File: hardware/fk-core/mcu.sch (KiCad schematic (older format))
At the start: 10 parts, among them P2 CONN_01X02, SW1 SPST-RESCUE-mcu, U1 ATSAMD21G-M, X1 XTAL-3.2X1.5

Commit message: Adding GPS connector and BOM placeholder.
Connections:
- net GPS_RX: now reaches U1.37 (PB22(SER5:2+))
- net GPX_TS: now reaches U1.38 (PB23(SER5:3+))
- no-connect marks 26 -> 24
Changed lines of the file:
@@
 LIBS:tps63060
 LIBS:max1704xx
+LIBS:gp-635tsmd
 LIBS:fk-core-cache
 EELAYER 25 0
@@
 	2350 2700 2400 2700
 $Comp
-L GND #PWR4
+L GND #PWR01
 U 1 1 587F9BAD
 P 2850 1900
-F 0 "#PWR4" H 2850 1650 50  0001 C CNN
+F 0 "#PWR01" H 2850 1650 50  0001 C CNN
 F 1 "GND" H 2850 1750 50  0000 C CNN
 F 2 "" H 2850 1900 50  0000 C CNN
@@
 $EndComp
 $Comp
-L GND #PWR3
+L GND #PWR02
 U 1 1 587F9BCB
 P 2350 1900
-F 0 "#PWR3" H 2350 1650 50  0001 C CNN
+F 0 "#PWR02" H 2350 1650 50  0001 C CNN
 F 1 "GND" H 2350 1750 50  0000 C CNN
 F 2 "" H 2350 1900 50  0000 C CNN
@@
 Connection ~ 2350 2700
 $Comp
-L +3V3 #PWR5
+L +3V3 #PWR03
 U 1 1 587F9D09
 P 3350 1900
-F 0 "#PWR5" H 3350 1750 50  0001 C CNN
+F 0 "#PWR03" H 3350 1750 50  0001 C CNN
 F 1 "+3V3" H 3350 2040 50  0000 C CNN
 F 2 "" H 3350 1900 50  0000 C CNN
@@
 	3700 2550 3700 2650
 $Comp
-L GND #PWR6
+L GND #PWR04
 U 1 1 587F9D9D
 P 3700 3000
-F 0 "#PWR6" H 3700 2750 50  0001 C CNN
+F 0 "#PWR04" H 3700 2750 50  0001 C CNN
 F 1 "GND" H 3700 2850 50  0000 C CNN
 F 2 "" H 3700 3000 50  0000 C CNN
@@
 	3300 1450 3800 1450
 $Comp
-L GND #PWR8
+L GND #PWR05
 U 1 1 587F9FB0
 P 5150 1450
-F 0 "#PWR8" H 5150 1200 50  0001 C CNN
+F 0 "#PWR05" H 5150 1200 50  0001 C CNN
 F 1 "GND" H 5150 1300 50  0000 C CNN
 F 2 "" H 5150 1450 50  0000 C CNN
@@
 	5150 1450 4800 1450
 $Comp
-L +3V3 #PWR9
+L +3V3 #PWR06
 U 1 1 587FA095
 P 7250 1900
-F 0 "#PWR9" H 7250 1750 50  0001 C CNN
+F 0 "#PWR06" H 7250 1750 50  0001 C CNN
 F 1 "+3V3" H 7250 2040 50  0000 C CNN
 F 2 "" H 7250 1900 50  0000 C CNN
@@
 	6900 2650 7750 2650
 $Comp
-L GND #PWR7
+L GND #PWR07
 U 1 1 587FABBF
 P 3750 5650
-F 0 "#PWR7" H 3750 5400 50  0001 C CNN
+F 0 "#PWR07" H 3750 5400 50  0001 C CNN
 F 1 "GND" H 3750 5500 50  0000 C CNN
 F 2 "" H 3750 5650 50  0000 C CNN
@@
 SCL1
 $Comp
-L +3V3 #PWR10
+L +3V3 #PWR08
 U 1 1 587FE0E2
 P 9850 3800
-F 0 "#PWR10" H 9850 3650 50  0001 C CNN
+F 0 "#PWR08" H 9850 3650 50  0001 C CNN
 F 1 "+3V3" H 9850 3940 50  0000 C CNN
 F 2 "" H 9850 3800 50  0000 C CNN
@@
 $EndComp
 $Comp
-L +3V3 #PWR11
+L +3V3 #PWR09
 U 1 1 587FE165
 P 9850 4000
-F 0 "#PWR11" H 9850 3850 50  0001 C CNN
+F 0 "#PWR09" H 9850 3850 50  0001 C CNN
 F 1 "+3V3" H 9850 4140 50  0000 C CNN
 F 2 "" H 9850 4000 50  0000 C CNN
@@
 NoConn ~ 6900 4450
 NoConn ~ 6900 4550
-NoConn ~ 7700 5250
-NoConn ~ 7700 5150
 NoConn ~ 4200 4650
 NoConn ~ 4200 4550
@@
 NoConn ~ 4200 3750
 $Comp
-L PWR_FLAG #FLG1
+L PWR_FLAG #FLG010
 U 1 1 5880FC74
 P 3300 1300
-F 0 "#FLG1" H 3300 1395 50  0001 C CNN
+F 0 "#FLG010" H 3300 1395 50  0001 C CNN
 F 1 "PWR_FLAG" H 3300 1480 50  0000 C CNN
 F 2 "" H 3300 1300 50  0000 C CNN
@@
 $EndComp
 $Comp
-L +3V3 #PWR1
+L +3V3 #PWR011
 U 1 1 58811F88
 P 1800 1900
-F 0 "#PWR1" H 1800 1750 50  0001 C CNN
+F 0 "#PWR011" H 1800 1750 50  0001 C CNN
 F 1 "+3V3" H 1800 2040 50  0000 C CNN
 F 2 "" H 1800 1900 50  0000 C CNN
@@
 $EndComp
 $Comp
-L GND #PWR2
+L GND #PWR012
 U 1 1 58811FC0
 P 1800 2700
-F 0 "#PWR2" H 1800 2450 50  0001 C CNN
+F 0 "#PWR012" H 1800 2450 50  0001 C CNN
 F 1 "GND" H 1800 2550 50  0000 C CNN
 F 2 "" H 1800 2700 50  0000 C CNN
@@
 $EndComp
 NoConn ~ 6900 3350
+Text GLabel 7700 5150 2    60   Input ~ 0
+GPS_RX
+Text GLabel 7700 5250 2    60   Input ~ 0
+GPX_TS
 $EndSCHEMATC

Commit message: Assigning most of the footprints.
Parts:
- C1, C10, C2, C3: footprint (none) -> Capacitors_SMD:C_0805_HandSoldering
- P2: footprint (none) -> Socket_Strips:Socket_Strip_Straight_1x02
- R1, R2: footprint (none) -> Resistors_SMD:R_0805_HandSoldering
- SW1: footprint (none) -> Buttons_Switches_SMD:SW_SPST_KMR2
- U1: footprint SparkFun-DigitalIC_QFN-48 -> Housings_QFP:TQFP-48-1EP_7x7mm_Pitch0.5mm
- X1: footprint XTAL3215 -> Crystals:Crystal_SMD_G8-2pin_3.2x1.5mm_HandSoldering
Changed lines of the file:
@@
 F 0 "U1" H 4300 5860 45  0000 L BNN
 F 1 "ATSAMD21G-M" H 4300 2740 45  0000 L BNN
-F 2 "SparkFun-DigitalIC_QFN-48" H 5530 4200 20  0001 C CNN
+F 2 "Housings_QFP:TQFP-48-1EP_7x7mm_Pitch0.5mm" H 5530 4200 20  0001 C CNN
 F 3 "http://www.atmel.com/Images/Atmel-42181-SAM-D21_Datasheet.pdf" H 5500 4050 60  0001 C CNN
 F 4 "ATSAMD21G18A-AUTCT-ND" H 5500 4050 60  0001 C CNN "SPN"
@@
 F 0 "X1" H 2500 2850 45  0000 L BNN
 F 1 "XTAL-3.2X1.5" H 2450 2500 45  0000 L BNN
-F 2 "XTAL3215" H 2630 2850 20  0001 C CNN
+F 2 "Crystals:Crystal_SMD_G8-2pin_3.2x1.5mm_HandSoldering" H 2630 2850 20  0001 C CNN
 F 3 "" H 2600 2700 60  0001 C CNN
 F 4 "644-1156-1-ND" H 2600 2700 60  0001 C CNN "SPN"
@@
 F 0 "C1" H 2375 2350 50  0000 L CNN
 F 1 "22pF" H 2375 2150 50  0000 L CNN
-F 2 "" H 2388 2100 50  0000 C CNN
+F 2 "Capacitors_SMD:C_0805_HandSoldering" H 2388 2100 50  0001 C CNN
 F 3 "" H 2350 2250 50  0000 C CNN
 F 4 "399-1113-1-ND" H 2350 2250 60  0001 C CNN "SPN"
@@
 F 0 "C2" H 2875 2350 50  0000 L CNN
 F 1 "22pF" H 2875 2150 50  0000 L CNN
-F 2 "" H 2888 2100 50  0000 C CNN
+F 2 "Capacitors_SMD:C_0805_HandSoldering" H 2888 2100 50  0001 C CNN
 F 3 "" H 2850 2250 50  0000 C CNN
 F 4 "399-1113-1-ND" H 2850 2250 60  0001 C CNN "SPN"
@@
 F 0 "C3" H 3725 2900 50  0000 L CNN
 F 1 "1uF" H 3725 2700 50  0000 L CNN
-F 2 "" H 3738 2650 50  0000 C CNN
+F 2 "Capacitors_SMD:C_0805_HandSoldering" H 3738 2650 50  0001 C CNN
 F 3 "" H 3700 2800 50  0000 C CNN
 F 4 "490-1320-1-ND" H 3700 2800 60  0001 C CNN "SPN"
@@
 F 0 "SW1" H 4300 1550 50  0000 C CNN
 F 1 "SPST-RESCUE-mcu" H 4300 1350 50  0000 C CNN
-F 2 "" H 4300 1450 50  0000 C CNN
+F 2 "Buttons_Switches_SMD:SW_SPST_KMR2" H 4300 1450 50  0001 C CNN
 F 3 "" H 4300 1450 50  0000 C CNN
 F 4 "401-1426-1-ND" H 4300 1450 60  0001 C CNN "SPN"
@@
 F 0 "R1" V 9630 3800 50  0000 C CNN
 F 1 "10k" V 9550 3800 50  0000 C CNN
-F 2 "" V 9480 3800 50  0000 C CNN
+F 2 "Resistors_SMD:R_0805_HandSoldering" V 9480 3800 50  0001 C CNN
 F 3 "" H 9550 3800 50  0000 C CNN
 F 4 "541-10.0KCCT-ND" H 9550 3800 60  0001 C CNN "SPN"
@@
 F 0 "R2" V 9630 4000 50  0000 C CNN
 F 1 "10k" V 9550 4000 50  0000 C CNN
-F 2 "" V 9480 4000 50  0000 C CNN
+F 2 "Resistors_SMD:R_0805_HandSoldering" V 9480 4000 50  0001 C CNN
 F 3 "" H 9550 4000 50  0000 C CNN
 F 4 "541-10.0KCCT-ND" H 9550 4000 60  0001 C CNN "SPN"
@@
 F 0 "P2" H 8250 4850 50  0000 C CNN
 F 1 "CONN_01X02" V 8350 4700 50  0000 C CNN
-F 2 "" H 8250 4700 50  0000 C CNN
+F 2 "Socket_Strips:Socket_Strip_Straight_1x02" H 8250 4700 50  0001 C CNN
 F 3 "" H 8250 4700 50  0000 C CNN
 	1    8250 4700
@@
 F 0 "C10" H 1825 2350 50  0000 L CNN
 F 1 "10uF" H 1825 2150 50  0000 L CNN
-F 2 "" H 1838 2100 50  0000 C CNN
+F 2 "Capacitors_SMD:C_0805_HandSoldering" H 1838 2100 50  0001 C CNN
 F 3 "" H 1800 2250 50  0000 C CNN
 F 4 "490-1718-1-ND" H 1800 2250 60  0001 C CNN "SPN"

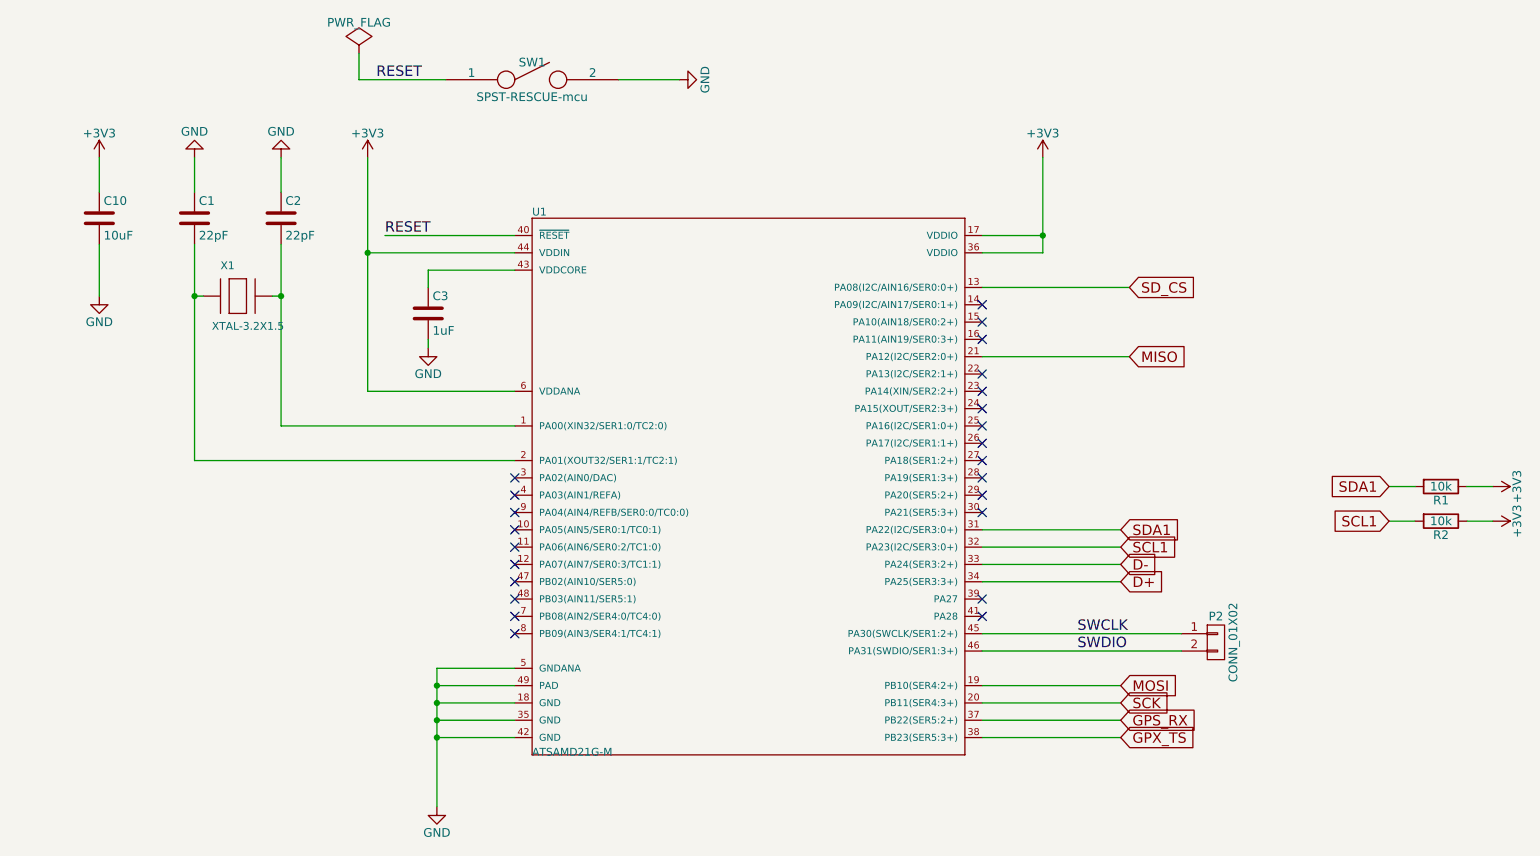
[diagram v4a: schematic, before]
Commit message: Adding a neopixel, maybe gonna use it. Also some more jumpers.
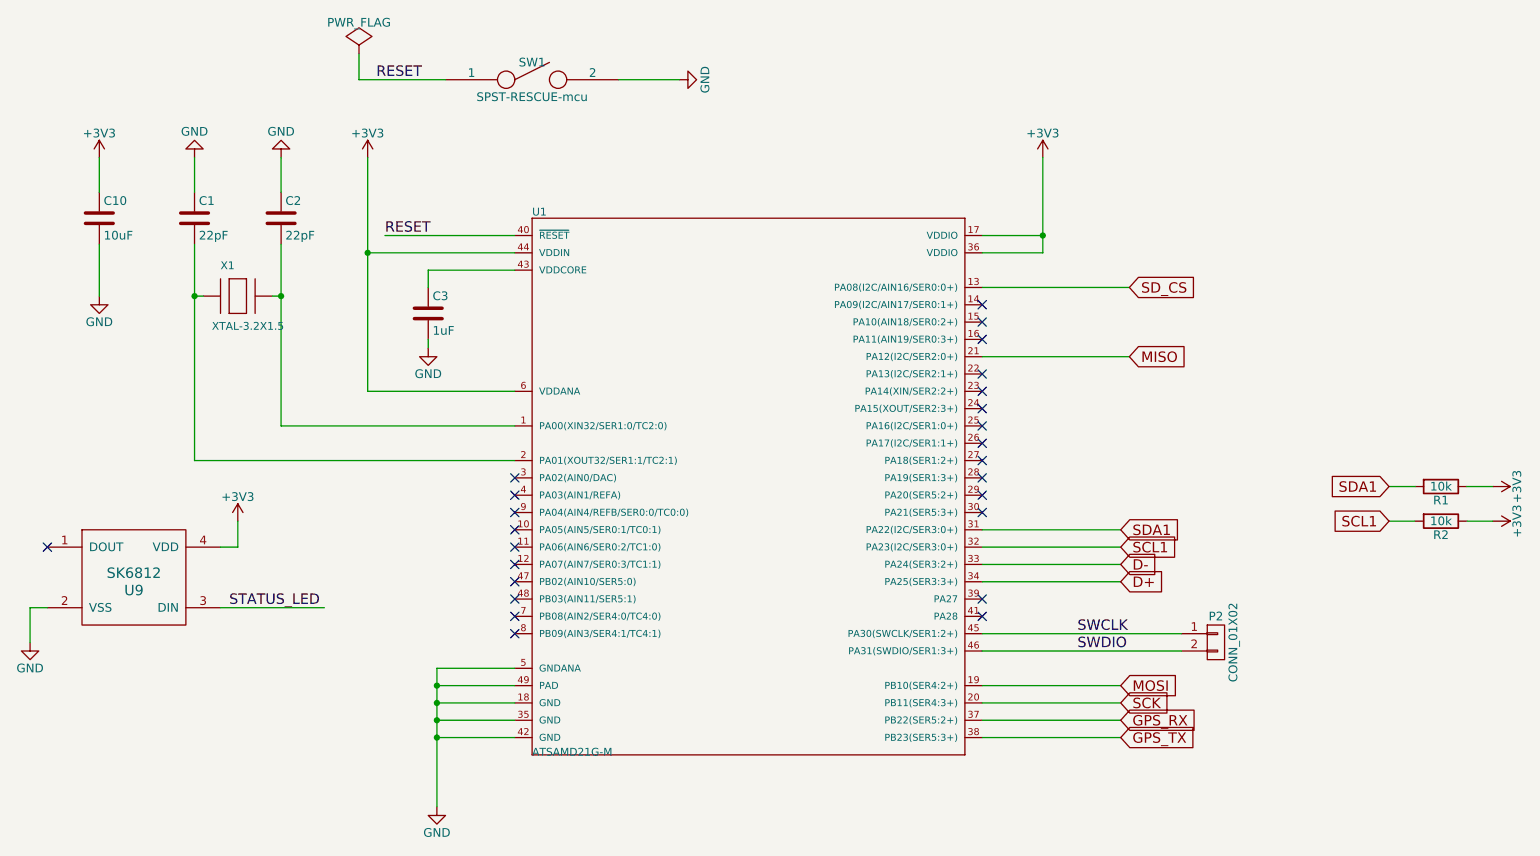
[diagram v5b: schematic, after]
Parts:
- added U9: SK6812, SOJ-4:SOJ-4, symbol SK6812
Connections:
- net +3V3: now also U9.4 (VDD)
- net GND: now also U9.2 (VSS)
- net GPX_TS renamed GPS_TX
- new net STATUS_LED: U9.3 (DIN)
- no-connect marks 24 -> 25
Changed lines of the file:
@@
 LIBS:gp-635tsmd
 LIBS:fgpmmopa6h
+LIBS:sk6812
 LIBS:fk-core-cache
 EELAYER 25 0
@@
 $EndComp
 Wire Wire Line
-	6900 2450 7250 2450
-Wire Wire Line
-	7250 2450 7250 1900
+	7250 2450 6900 2450
+Wire Wire Line
+	7250 1900 7250 2450
 Wire Wire Line
 	6900 2350 7250 2350
@@
 $EndComp
 Wire Wire Line
-	3750 5650 3750 4850
+	3750 4850 3750 5650
 Wire Wire Line
 	3750 4850 4200 4850
@@
 GPS_RX
 Text GLabel 7700 5250 2    60   Input ~ 0
-GPX_TS
+GPS_TX
+$Comp
+L SK6812 U9
+U 1 1 5880C549
+P 2000 4300
+F 0 "U9" H 2000 4200 60  0000 C CNN
+F 1 "SK6812" H 2000 4300 60  0000 C CNN
+F 2 "SOJ-4:SOJ-4" H 2000 4300 60  0001 C CNN
+F 3 "" H 2000 4300 60  0001 C CNN
+	1    2000 4300
+	1    0    0    -1
+$EndComp
+$Comp
+L GND #PWR013
+U 1 1 5880C5B1
+P 1400 4700
+F 0 "#PWR013" H 1400 4450 50  0001 C CNN
+F 1 "GND" H 1400 4550 50  0000 C CNN
+F 2 "" H 1400 4700 50  0000 C CNN
+F 3 "" H 1400 4700 50  0000 C CNN
+	1    1400 4700
+	1    0    0    -1
+$EndComp
+Wire Wire Line
+	1500 4500 1400 4500
+Wire Wire Line
+	1400 4500 1400 4700
+NoConn ~ 1500 4150
+$Comp
+L +3V3 #PWR014
+U 1 1 5880C639
+P 2600 4000
+F 0 "#PWR014" H 2600 3850 50  0001 C CNN
+F 1 "+3V3" H 2600 4140 50  0000 C CNN
+F 2 "" H 2600 4000 50  0000 C CNN
+F 3 "" H 2600 4000 50  0000 C CNN
+	1    2600 4000
+	1    0    0    -1
+$EndComp
+Wire Wire Line
+	2600 4000 2600 4150
+Wire Wire Line
+	2600 4150 2500 4150
+Wire Wire Line
+	2500 4500 3100 4500
+Text Label 2550 4500 0    60   ~ 0
+STATUS_LED
 $EndSCHEMATC

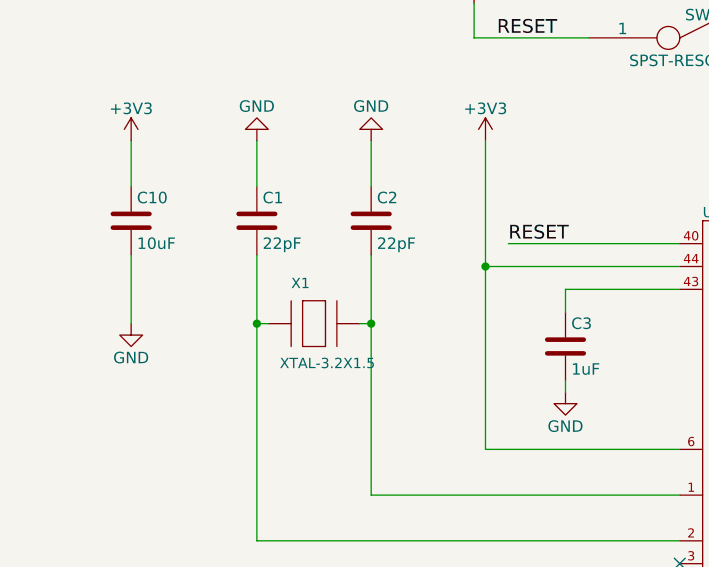
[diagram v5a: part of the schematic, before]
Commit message: Cleaning up footprints and libraries.
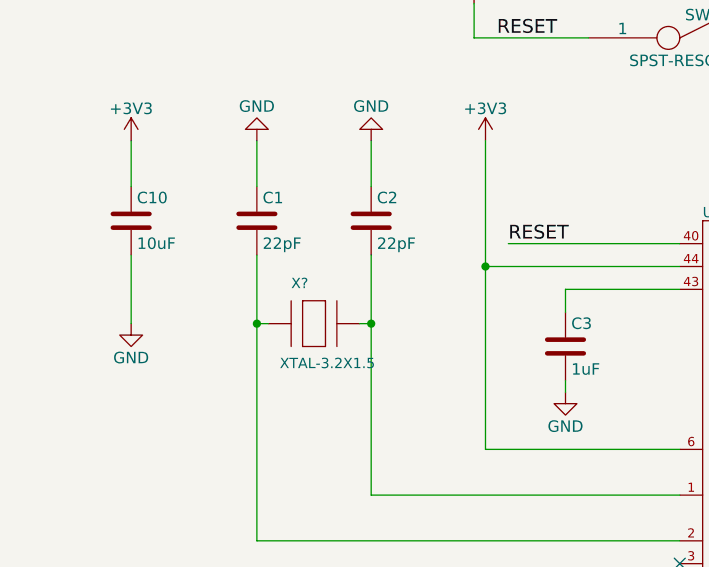
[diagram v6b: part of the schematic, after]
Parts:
- removed X1: XTAL-3.2X1.5, Crystals:Crystal_SMD_G8-2pin_3.2x1.5mm_HandSoldering, symbol XTAL-3.2X1.5
- added X?: XTAL-3.2X1.5, XTAL3215, symbol XTAL-3.2X1.5
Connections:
- net at C2.2, U1.1 (PA00(XIN32/SER1:0/TC2:0)): now also X?.2
- net at C1.2, U1.2 (PA01(XOUT32/SER1:1/TC2:1)): now also X?.1
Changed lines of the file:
@@
 LIBS:microsd
 LIBS:pcf8523t
-LIBS:xtal32x15
 LIBS:tps63060
 LIBS:max1704xx
@@
 LIBS:fgpmmopa6h
 LIBS:sk6812
+LIBS:dcbarrelsmt
+LIBS:xtal-3.2x1
 LIBS:fk-core-cache
 EELAYER 25 0
@@
 F 4 "ATSAMD21G18A-AUTCT-ND" H 5500 4050 60  0001 C CNN "SPN"
 	1    5500 4050
-	1    0    0    -1
-$EndComp
-$Comp
-L XTAL-3.2X1.5 X1
-U 1 1 587F997C
-P 2600 2700
-F 0 "X1" H 2500 2850 45  0000 L BNN
-F 1 "XTAL-3.2X1.5" H 2450 2500 45  0000 L BNN
-F 2 "Crystals:Crystal_SMD_G8-2pin_3.2x1.5mm_HandSoldering" H 2630 2850 20  0001 C CNN
-F 3 "" H 2600 2700 60  0001 C CNN
-F 4 "644-1156-1-ND" H 2600 2700 60  0001 C CNN "SPN"
-	1    2600 2700
 	1    0    0    -1
 $EndComp
@@
 Text Label 2550 4500 0    60   ~ 0
 STATUS_LED
+$Comp
+L XTAL-3.2X1.5 X?
+U 1 1 5880F630
+P 2600 2700
+F 0 "X?" H 2500 2850 45  0000 L BNN
+F 1 "XTAL-3.2X1.5" H 2450 2500 45  0000 L BNN
+F 2 "XTAL3215" H 2630 2850 20  0001 C CNN
+F 3 "" H 2600 2700 60  0001 C CNN
+	1    2600 2700
+	1    0    0    -1
+$EndComp
 $EndSCHEMATC

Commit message: Adding SMA footprint for GPS and fix XTAL.
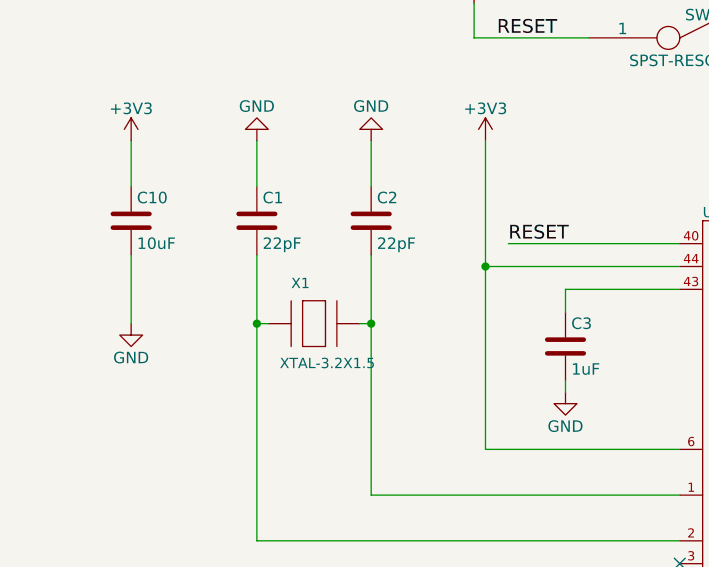
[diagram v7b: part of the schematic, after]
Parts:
- X1: renamed from X?; footprint XTAL3215 -> Crystals:Crystal_SMD_G8-2pin_3.2x1.5mm_HandSoldering
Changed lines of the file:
@@
 STATUS_LED
 $Comp
-L XTAL-3.2X1.5 X?
+L XTAL-3.2X1.5 X1
 U 1 1 5880F630
 P 2600 2700
-F 0 "X?" H 2500 2850 45  0000 L BNN
+F 0 "X1" H 2500 2850 45  0000 L BNN
 F 1 "XTAL-3.2X1.5" H 2450 2500 45  0000 L BNN
-F 2 "XTAL3215" H 2630 2850 20  0001 C CNN
+F 2 "Crystals:Crystal_SMD_G8-2pin_3.2x1.5mm_HandSoldering" H 2630 2850 20  0001 C CNN
 F 3 "" H 2600 2700 60  0001 C CNN
 	1    2600 2700
